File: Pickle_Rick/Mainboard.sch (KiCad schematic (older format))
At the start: 81 parts, among them J10 Conn_01x02_Male, J12 Conn_01x02_Male, J13 Conn_01x02, J2 8P8C_LED, J3 Micro_SD_Card_Det, J9 Conn_01x02_Male, Q1 MMDT2222A, Q3 PMV20ENR, U1 CP2102N-A01-GQFN24, U10 PCA9536D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

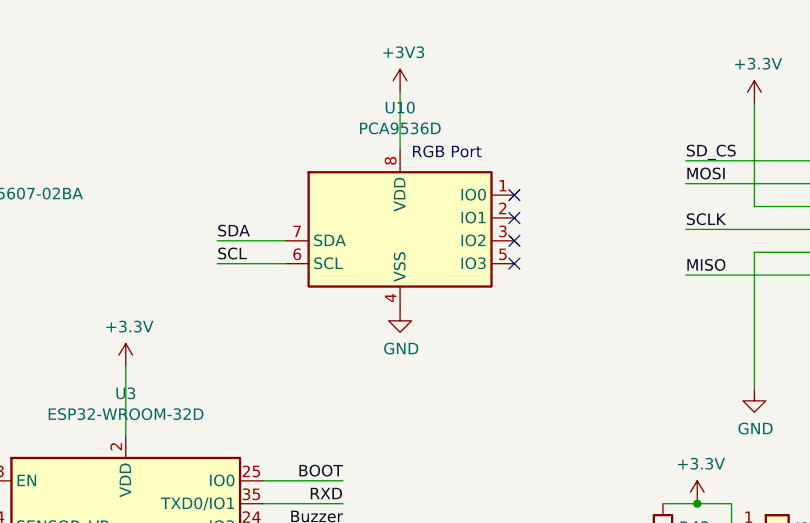
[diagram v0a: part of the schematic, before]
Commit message: fixed rbg port
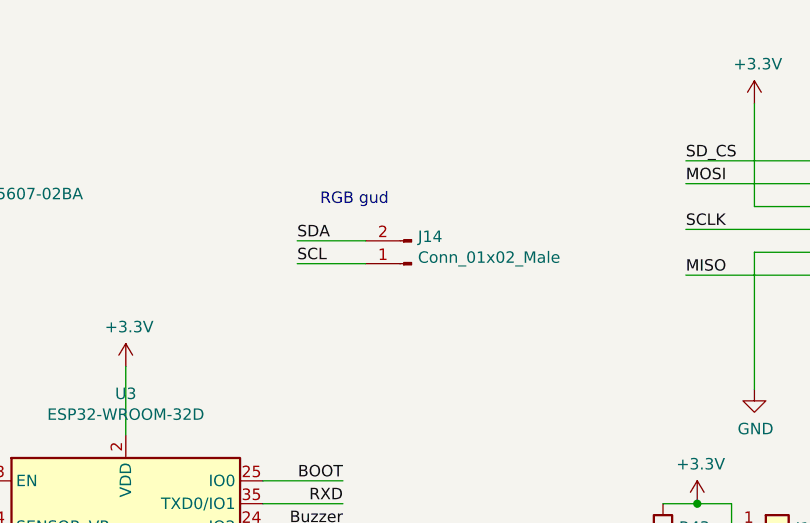
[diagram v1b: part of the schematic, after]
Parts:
- removed U10: PCA9536D, Package_SO:SOIC-8_3.9x4.9mm_P1.27mm, symbol Interface_Expansion:PCA9536D
- added J14: Conn_01x02_Male, Connector_PinHeader_2.54mm:PinHeader_1x02_P2.54mm_Vertical, symbol Connector:Conn_01x02_Male
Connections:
- net SCL: now also J14.1 (Pin_1)
- net SDA: now also J14.2 (Pin_2)
- no-connect marks 28 -> 24
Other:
- note added: "RGB gud"
- note removed: "RGB Port"
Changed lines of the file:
@@
 	-1   0    0    1
 $EndComp
-$Comp
-L Interface_Expansion:PCA9536D U10
-U 1 1 60497087
-P 7450 1400
-F 0 "U10" H 7450 1881 50  0000 C CNN
-F 1 "PCA9536D" H 7450 1790 50  0000 C CNN
-F 2 "Package_SO:SOIC-8_3.9x4.9mm_P1.27mm" H 8450 1050 50  0001 C CNN
-F 3 "http://www.nxp.com/documents/data_sheet/PCA9536.pdf" H 7250 -300 50  0001 C CNN
-	1    7450 1400
-	1    0    0    -1
-$EndComp
-$Comp
-L power:+3V3 #PWR0111
-U 1 1 604BFA09
-P 7450 850
-F 0 "#PWR0111" H 7450 700 50  0001 C CNN
-F 1 "+3V3" H 7465 1023 50  0000 C CNN
-F 2 "" H 7450 850 50  0001 C CNN
-F 3 "" H 7450 850 50  0001 C CNN
-	1    7450 850
-	1    0    0    -1
-$EndComp
-$Comp
-L power:GND #PWR0112
-U 1 1 604C1D4C
-P 7450 1800
-F 0 "#PWR0112" H 7450 1550 50  0001 C CNN
-F 1 "GND" H 7455 1627 50  0000 C CNN
-F 2 "" H 7450 1800 50  0001 C CNN
-F 3 "" H 7450 1800 50  0001 C CNN
-	1    7450 1800
-	1    0    0    -1
-$EndComp
-Wire Wire Line
-	7450 850  7450 1100
-Text Notes 7500 1150 0    50   ~ 0
-RGB Port
-NoConn ~ 7950 1300
-NoConn ~ 7950 1400
-NoConn ~ 7950 1500
-NoConn ~ 7950 1600
-Wire Wire Line
-	6950 1500 6650 1500
-Wire Wire Line
-	6950 1600 6650 1600
-Text Label 6650 1500 0    50   ~ 0
+Text Notes 7100 1350 0    50   ~ 0
+RGB gud
+Wire Wire Line
+	7300 1500 7000 1500
+Wire Wire Line
+	7300 1600 7000 1600
+Text Label 7000 1500 0    50   ~ 0
 SDA
-Text Label 6650 1600 0    50   ~ 0
+Text Label 7000 1600 0    50   ~ 0
 SCL
 $Comp
@@
 Wire Wire Line
 	8900 2850 8900 2950
+$Comp
+L Connector:Conn_01x02_Male J14
+U 1 1 60A8850A
+P 7500 1600
+F 0 "J14" H 7472 1482 50  0000 R CNN
+F 1 "Conn_01x02_Male" H 7472 1573 50  0000 R CNN
+F 2 "Connector_PinHeader_2.54mm:PinHeader_1x02_P2.54mm_Vertical" H 7500 1600 50  0001 C CNN
+F 3 "~" H 7500 1600 50  0001 C CNN
+	1    7500 1600
+	-1   0    0    1
+$EndComp
 $EndSCHEMATC
